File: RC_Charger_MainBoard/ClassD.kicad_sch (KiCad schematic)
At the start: 25 parts, among them J3 SPK1, J4 SPK2, U13 TAS5825MRHB

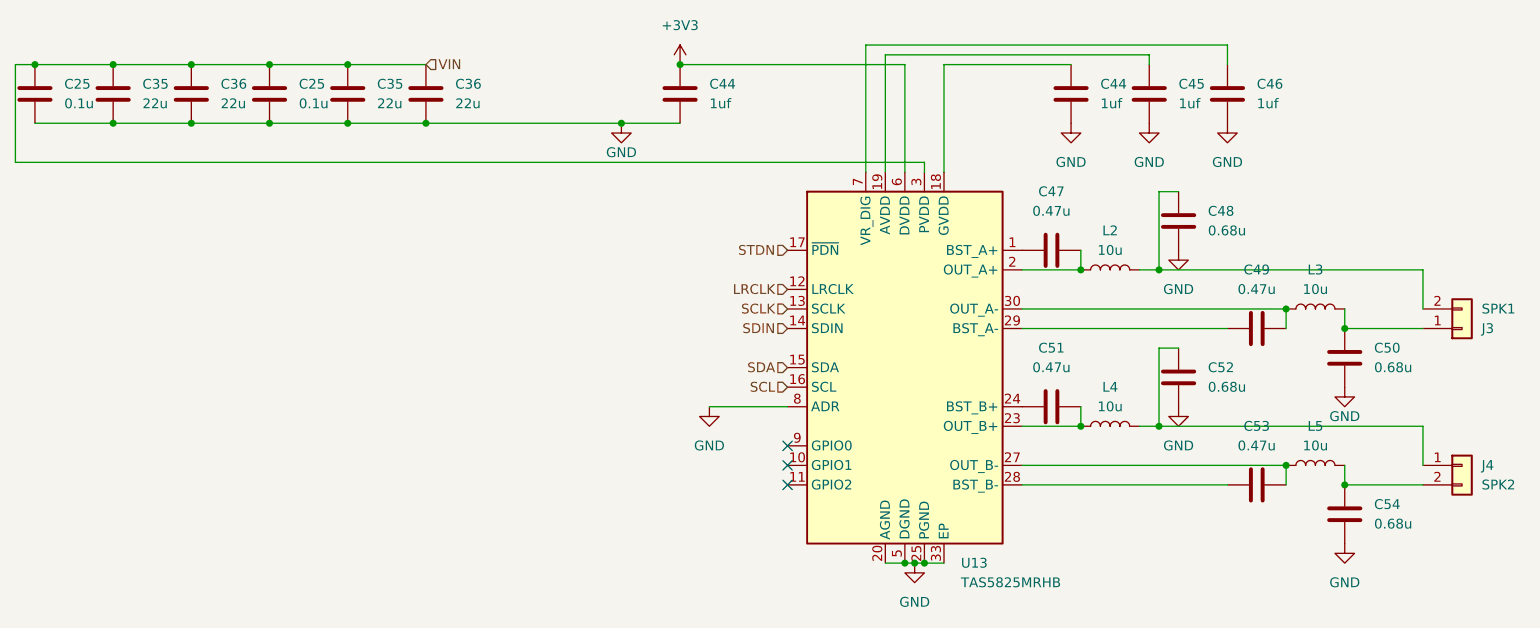
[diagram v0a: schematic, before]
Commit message: Change components for costdown
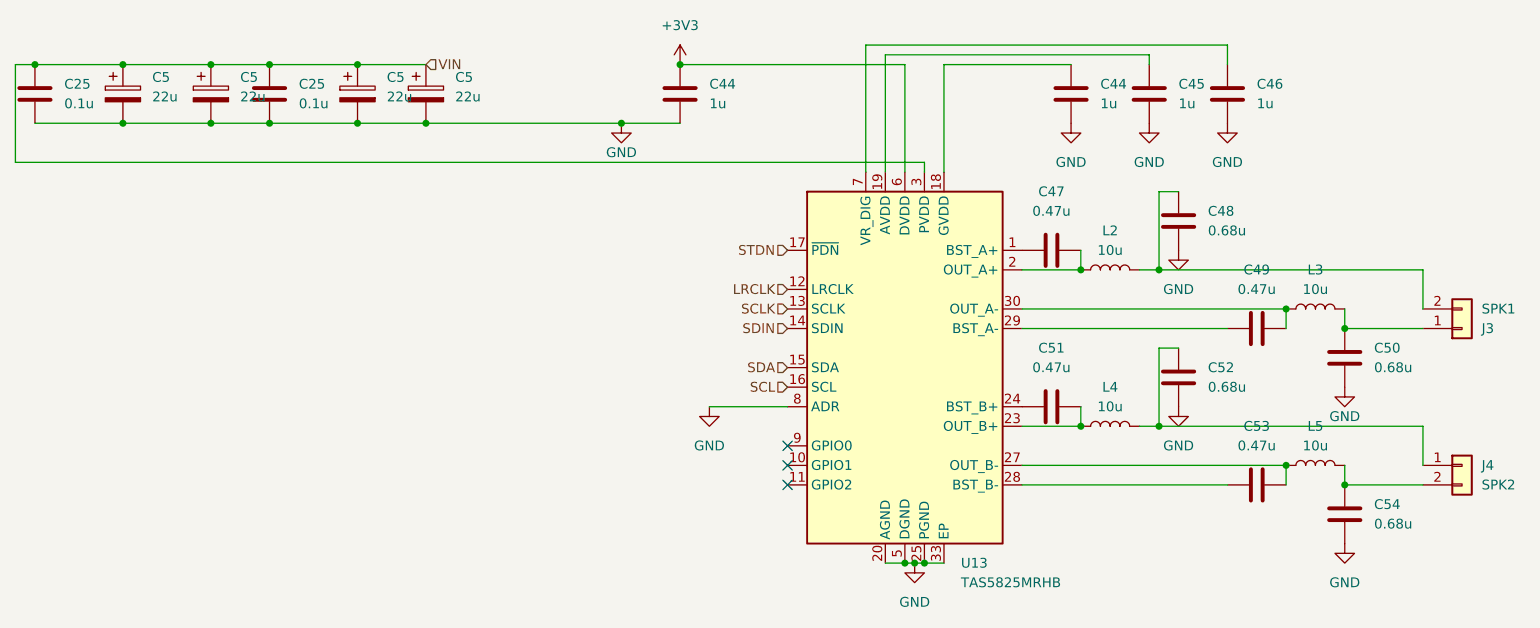
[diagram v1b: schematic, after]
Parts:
- removed C35 (x2), C36 (x2): 22u, Capacitor_SMD:C_2220_5650Metric, symbol Device:C
- added C5 (x4): 22u, Capacitor_SMD:CP_Elec_6.3x5.4, symbol Device:C_Polarized
- C44, C45, C46: value 1uf -> 1u
- L2, L3, L4, L5: footprint Inductor_SMD:L_Bourns_SRP7028A_7.3x6.6mm -> Inductor_SMD:L_Taiyo-Yuden_NR-50xx_HandSoldering
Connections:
- net GND: now also C5.2, C5.2, C5.2, C5.2
- net VIN: now also C5.1, C5.1, C5.1, C5.1
